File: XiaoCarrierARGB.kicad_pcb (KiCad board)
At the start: 2 copper layers, 76.4 x 50.8 mm, 24 parts, among them J1 V_{IN}^{10-24V}, J2 Conn_01x08, J3 Conn_01x01, J4 Conn_01x08, J5 Conn_01x01, J6 Conn_01x06, U1 TLV75733PDBV, U2 TPP362083-T6TR, U3 XIAO-ESP32-C6-DIP, U4 74LVC1T45W6-7, U5 74LVC1T45W6-7, U6 74LVC1T45W6-7

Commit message: adjusted prelim layout
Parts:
- moved U4 35.2 mm to (131.8, 113.3)
- moved U5 35.0 mm to (131.8, 108.5)
- moved U6 35.0 mm to (131.8, 103.6)
- moved C4 33.4 mm to (114.2, 93.5), turned to 90 degrees
- moved J6 33.2 mm to (148.8, 105.0)
- moved J4 32.4 mm to (125.2, 83.0)
- moved U3 32.0 mm to (117.4, 106.6)
- moved J3 30.1 mm to (121.2, 83.0)
- moved U1 29.3 mm to (118.1, 93.6), turned to 0 degrees
- moved F1 28.2 mm to (93.2, 100.0)
- moved J2 28.1 mm to (99.5, 83.0)
- moved J5 27.1 mm to (95.2, 83.0)
- moved D1 27.0 mm to (102.8, 108.0)
- moved R2 26.3 mm to (98.3, 101.5), turned to 180 degrees
- moved C1 25.8 mm to (121.8, 93.5), turned to -90 degrees
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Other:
- board size 76.4 x 50.8 mm -> 63.5 x 38.1 mm

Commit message: moved to 4 layers
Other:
- copper layers 2 -> 4
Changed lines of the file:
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@@
 	(layers
 		(0 "F.Cu" signal)
+		(4 "In1.Cu" power)
+		(6 "In2.Cu" power)
 		(2 "B.Cu" signal)
 		(9 "F.Adhes" user "F.Adhesive")
@@
 			)
 			(layer "dielectric 1"
+				(type "prepreg")
+				(thickness 0.1)
+				(material "FR4")
+				(epsilon_r 4.5)
+				(loss_tangent 0.02)
+			)
+			(layer "In1.Cu"
+				(type "copper")
+				(thickness 0.035)
+			)
+			(layer "dielectric 2"
 				(type "core")
-				(thickness 1.51)
+				(thickness 1.24)
+				(material "FR4")
+				(epsilon_r 4.5)
+				(loss_tangent 0.02)
+			)
+			(layer "In2.Cu"
+				(type "copper")
+				(thickness 0.035)
+			)
+			(layer "dielectric 3"
+				(type "prepreg")
+				(thickness 0.1)
 				(material "FR4")
 				(epsilon_r 4.5)
@@
 		(capping no)
 		(filling no)
+		(zone_defaults)
 		(grid_origin 88.25 119.05)
 		(pcbplotparams

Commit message: realigned schem grid added netclass assignment and net names
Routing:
- added copper zone on In1.Cu, net GND
- added copper zone on In2.Cu, net GND
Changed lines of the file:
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@@
 		(capping no)
 		(filling no)
-		(zone_defaults)
 		(grid_origin 88.25 119.05)
 		(pcbplotparams
@@
 		(layer "Edge.Cuts")
 	)
+	(zone
+		(net "GND")
+		(layers "In1.Cu" "In2.Cu")
+		(name "GND")
+		(hatch edge 0.5)
+		(connect_pads
+			(clearance 0.5)
+		)
+		(min_thickness 0.25)
+		(fill yes
+			(thermal_gap 0.5)
+			(thermal_bridge_width 0.5)
+			(island_removal_mode 0)
+		)
+		(polygon
+			(pts
+				(xy 85.25 77.55) (xy 152.75 77.55) (xy 152.75 120.55) (xy 85.75 120.55)
+			)
+		)
+	)
 	(embedded_fonts no)

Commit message: started prettying it up a bit
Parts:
- moved F1 0.45 mm to (92.8, 100.0)
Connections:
- net Net-(J1-Pin_1) renamed /V_{IN}
- net Net-(J2-Pin_3) renamed /GPIO17
- net Net-(J2-Pin_4) renamed /GPIO19
- net Net-(J2-Pin_7) renamed /GPIO20
- net Net-(J2-Pin_8) renamed /GPIO18
- net Net-(J4-Pin_3) renamed /GPIO16
- net Net-(J4-Pin_4) renamed /GPIO23
- net Net-(J4-Pin_7) renamed /GPIO22
- net Net-(J4-Pin_8) renamed /GPIO21
- net Net-(J6-Pin_1) renamed /LED_DATA^{1}
- net Net-(J6-Pin_3) renamed /LED_DATA^{2}
- net Net-(J6-Pin_5) renamed /LED_DATA^{3}
- net Net-(U2-EN) renamed /V_{IN}_{FUSED}
- net Net-(U2-SW) renamed /SWITCHNODE
- net Net-(U2-VBST) renamed /BOOTSTRAP
- net Net-(U2-VFB) renamed /FB_{BUCK}
- net Net-(U3-GPIO0_D0) renamed /GPIO0
- net Net-(U3-GPIO1_D1) renamed /GPIO1
- net Net-(U3-GPIO2_D2) renamed /GPIO2
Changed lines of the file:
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@@
 			(layers "F.Cu" "F.Mask" "F.Paste")
 			(roundrect_rratio 0.25)
-			(net "Net-(J6-Pin_3)")
+			(net "/LED_DATA^{2}")
 			(pinfunction "A_3")
 			(pintype "bidirectional")
@@
 			(layers "F.Cu" "F.Mask" "F.Paste")
 			(roundrect_rratio 0.25)
-			(net "Net-(U3-GPIO1_D1)")
+			(net "/GPIO1")
 			(pinfunction "B_4")
 			(pintype "bidirectional")
@@
 			(layers "*.Cu" "*.Mask")
 			(remove_unused_layers no)
-			(net "Net-(J1-Pin_1)")
+			(net "/V_{IN}")
 			(pinfunction "Pin_1_1")
 			(pintype "passive")
@@
 			(layers "F.Cu" "F.Mask" "F.Paste")
 			(roundrect_rratio 0.243902)
-			(net "Net-(U2-VFB)")
+			(net "/FB_{BUCK}")
 			(pintype "passive")
 		)
@@
 			(layers "F.Cu" "F.Mask" "F.Paste")
 			(roundrect_rratio 0.212766)
-			(net "Net-(U2-EN)")
+			(net "/V_{IN}_{FUSED}")
 			(pintype "passive")
 		)
@@
 			(layers "F.Cu" "F.Mask" "F.Paste")
 			(roundrect_rratio 0.125)
-			(net "Net-(U2-SW)")
+			(net "/SWITCHNODE")
 			(pinfunction "1_1")
 			(pintype "passive")
@@
 			(layers "*.Cu" "*.Mask")
 			(remove_unused_layers no)
-			(net "Net-(J4-Pin_3)")
+			(net "/GPIO16")
 			(pinfunction "Pin_3_3")
 			(pintype "passive")
@@
 			(layers "*.Cu" "*.Mask")
 			(remove_unused_layers no)
-			(net "Net-(J4-Pin_4)")
+			(net "/GPIO23")
 			(pinfunction "Pin_4_4")
 			(pintype "passive")
@@
 			(layers "*.Cu" "*.Mask")
 			(remove_unused_layers no)
-			(net "Net-(J4-Pin_7)")
+			(net "/GPIO22")
 			(pinfunction "Pin_7_7")
 			(pintype "passive")
@@
 			(layers "*.Cu" "*.Mask")
 			(remove_unused_layers no)
-			(net "Net-(J4-Pin_8)")
+			(net "/GPIO21")
 			(pinfunction "Pin_8_8")
 			(pintype "passive")
@@
 			(layers "*.Cu" "*.Mask")
 			(remove_unused_layers no)
-			(net "Net-(J2-Pin_3)")
+			(net "/GPIO17")
 			(pinfunction "Pin_3_3")
 			(pintype "passive")
@@
 			(layers "*.Cu" "*.Mask")
 			(remove_unused_layers no)
-			(net "Net-(J2-Pin_4)")
+			(net "/GPIO19")
 			(pinfunction "Pin_4_4")
 			(pintype "passive")
@@
 			(layers "*.Cu" "*.Mask")
 			(remove_unused_layers no)
-			(net "Net-(J2-Pin_7)")
+			(net "/GPIO20")
 			(pinfunction "Pin_7_7")
 			(pintype "passive")
@@
 			(layers "*.Cu" "*.Mask")
 			(remove_unused_layers no)
-			(net "Net-(J2-Pin_8)")
+			(net "/GPIO18")
 			(pinfunction "Pin_8_8")
 			(pintype "passive")
@@
 	(footprint "Fuse:Fuse_1812_4532Metric"
 		(layer "F.Cu")
-		(at 93.25 100.05 90)
+		(at 92.803052 100.05 90)
 		(descr "Fuse SMD 1812 (4532 Metric), square (rectangular) end terminal, IPC-7351 nominal, (Body size source: https://www.nikhef.nl/pub/departments/mt/projects/detectorR_D/dtddice/ERJ2G.pdf)")
 		(tags "fuse")
@@
 			(layers "F.Cu" "F.Mask" "F.Paste")
 			(roundrect_rratio 0.222222)
-			(net "Net-(J1-Pin_1)")
+			(net "/V_{IN}")
 			(pintype "passive")
 		)
@@
 			(layers "F.Cu" "F.Mask" "F.Paste")
 			(roundrect_rratio 0.222222)
-			(net "Net-(U2-EN)")
+			(net "/V_{IN}_{FUSED}")
 			(pintype "passive")
 		)
@@
 			(layers "F.Cu" "F.Mask" "F.Paste")
 			(roundrect_rratio 0.25)
-			(net "Net-(J6-Pin_5)")
+			(net "/LED_DATA^{3}")
 			(pinfunction "A_3")
 			(pintype "bidirectional")
@@
 			(layers "F.Cu" "F.Mask" "F.Paste")
 			(roundrect_rratio 0.25)
-			(net "Net-(U3-GPIO2_D2)")
+			(net "/GPIO2")
 			(pinfunction "B_4")
 			(pintype "bidirectional")
@@
 			(layers "F.Cu" "F.Mask" "F.Paste")
 			(roundrect_rratio 0.243902)
-			(net "Net-(U2-VFB)")
+			(net "/FB_{BUCK}")
 			(pintype "passive")
 		)
@@
 			(layers "F.Cu" "F.Mask")
 			(roundrect_rratio 0.1)
-			(net "Net-(U3-GPIO0_D0)")
+			(net "/GPIO0")
 			(pinfunction "GPIO0_D0_1")
 			(pintype "bidirectional")
@@
 			(layers "*.Cu" "*.Mask")
 			(remove_unused_layers no)
-			(net "Net-(U3-GPIO0_D0)")
+			(net "/GPIO0")
 			(pinfunction "GPIO0_D0_1")
 			(pintype "bidirectional")
@@
 			(layers "F.Cu" "F.Mask")
 			(roundrect_rratio 0.1)
-			(net "Net-(U3-GPIO1_D1)")
+			(net "/GPIO1")
 			(pinfunction "GPIO1_D1_2")
 			(pintype "bidirectional")
@@
 			(layers "*.Cu" "*.Mask")
 			(remove_unused_layers no)
-			(net "Net-(U3-GPIO1_D1)")
+			(net "/GPIO1")
 			(pinfunction "GPIO1_D1_2")
 			(pintype "bidirectional")
@@
 			(layers "F.Cu" "F.Mask")
 			(roundrect_rratio 0.1)
-			(net "Net-(U3-GPIO2_D2)")
+			(net "/GPIO2")
 			(pinfunction "GPIO2_D2_3")
 			(pintype "bidirectional")
@@
 			(layers "*.Cu" "*.Mask")
 			(remove_unused_layers no)
-			(net "Net-(U3-GPIO2_D2)")
+			(net "/GPIO2")
 			(pinfunction "GPIO2_D2_3")
 			(pintype "bidirectional")
@@
 			(layers "F.Cu" "F.Mask")
 			(roundrect_rratio 0.1)
-			(net "Net-(J4-Pin_8)")
+			(net "/GPIO21")
 			(pinfunction "GPIO21_D3_4")
 			(pintype "passive")
@@
 			(layers "*.Cu" "*.Mask")
 			(remove_unused_layers no)
-			(net "Net-(J4-Pin_8)")
+			(net "/GPIO21")
 			(pinfunction "GPIO21_D3_4")
 			(pintype "passive")
@@
 			(layers "F.Cu" "F.Mask")
 			(roundrect_rratio 0.1)
-			(net "Net-(J4-Pin_7)")
+			(net "/GPIO22")
 			(pinfunction "GPIO22_D4_5")
 			(pintype "bidirectional")
@@
 			(layers "*.Cu" "*.Mask")
 			(remove_unused_layers no)
-			(net "Net-(J4-Pin_7)")
+			(net "/GPIO22")
 			(pinfunction "GPIO22_D4_5")
 			(pintype "bidirectional")
@@
 			(layers "F.Cu" "F.Mask")
 			(roundrect_rratio 0.1)
-			(net "Net-(J4-Pin_4)")
+			(net "/GPIO23")
 			(pinfunction "GPIO23_D5_6")
 			(pintype "bidirectional")
@@
 			(layers "*.Cu" "*.Mask")
 			(remove_unused_layers no)
-			(net "Net-(J4-Pin_4)")
+			(net "/GPIO23")
 			(pinfunction "GPIO23_D5_6")
 			(pintype "bidirectional")
@@
 			(layers "F.Cu" "F.Mask")
 			(roundrect_rratio 0.1)
-			(net "Net-(J4-Pin_3)")
+			(net "/GPIO16")
 			(pinfunction "GPIO16_D6_7")
 			(pintype "bidirectional")
@@
 			(layers "*.Cu" "*.Mask")
 			(remove_unused_layers no)
-			(net "Net-(J4-Pin_3)")
+			(net "/GPIO16")
 			(pinfunction "GPIO16_D6_7")
 			(pintype "bidirectional")
@@
 			(layers "*.Cu" "*.Mask")
 			(remove_unused_layers no)
-			(net "Net-(J2-Pin_3)")
+			(net "/GPIO17")
 			(pinfunction "GPIO17_D7_8")
 			(pintype "bidirectional")
@@
 			(layers "F.Cu" "F.Mask")
 			(roundrect_rratio 0.1)
-			(net "Net-(J2-Pin_3)")
+			(net "/GPIO17")
 			(pinfunction "GPIO17_D7_8")
 			(pintype "bidirectional")
@@
 			(layers "*.Cu" "*.Mask")
 			(remove_unused_layers no)
-			(net "Net-(J2-Pin_4)")
+			(net "/GPIO19")
 			(pinfunction "GPIO19_D8_9")
 			(pintype "bidirectional")
@@
 			(layers "F.Cu" "F.Mask")
 			(roundrect_rratio 0.1)
-			(net "Net-(J2-Pin_4)")
+			(net "/GPIO19")
 			(pinfunction "GPIO19_D8_9")
 			(pintype "bidirectional")
@@
 			(layers "*.Cu" "*.Mask")
 			(remove_unused_layers no)
-			(net "Net-(J2-Pin_7)")
+			(net "/GPIO20")
 			(pinfunction "GPIO20_D9_10")
 			(pintype "bidirectional")
@@
 			(layers "F.Cu" "F.Mask")
 			(roundrect_rratio 0.1)
-			(net "Net-(J2-Pin_7)")
+			(net "/GPIO20")
 			(pinfunction "GPIO20_D9_10")
 			(pintype "bidirectional")
@@
 			(layers "*.Cu" "*.Mask")
 			(remove_unused_layers no)
-			(net "Net-(J2-Pin_8)")
+			(net "/GPIO18")
 			(pinfunction "GPIO18_D10_11")
 			(pintype "bidirectional")
@@
 			(layers "F.Cu" "F.Mask")
 			(roundrect_rratio 0.1)
-			(net "Net-(J2-Pin_8)")
+			(net "/GPIO18")
 			(pinfunction "GPIO18_D10_11")
 			(pintype "bidirectional")
@@
 			(layers "F.Cu" "F.Mask" "F.Paste")
 			(roundrect_rratio 0.25)
-			(net "Net-(J6-Pin_1)")
+			(net "/LED_DATA^{1}")
 			(pinfunction "A_3")
 			(pintype "bidirectional")
@@
 			(layers "F.Cu" "F.Mask" "F.Paste")
 			(roundrect_rratio 0.25)
-			(net "Net-(U3-GPIO0_D0)")
+			(net "/GPIO0")
 			(pinfunction "B_4")
 			(pintype "bidirectional")
@@
 			(layers "*.Cu" "*.Mask")
 			(remove_unused_layers no)
-			(net "Net-(J6-Pin_1)")
+			(net "/LED_DATA^{1}")
 			(pinfunction "Pin_1_1")
 			(pintype "passive")
@@
 			(layers "*.Cu" "*.Mask")
 			(remove_unused_layers no)
-			(net "Net-(J6-Pin_3)")
+			(net "/LED_DATA^{2}")
 			(pinfunction "Pin_3_3")
 			(pintype "passive")
@@
 			(layers "*.Cu" "*.Mask")
 			(remove_unused_layers no)
-			(net "Net-(J6-Pin_5)")
+			(net "/LED_DATA^{3}")
 			(pinfunction "Pin_5_5")
 			(pintype "passive")
@@
 			(layers "F.Cu" "F.Mask" "F.Paste")
 			(roundrect_rratio 0.25)
-			(net "Net-(U2-SW)")
+			(net "/SWITCHNODE")
 			(pinfunction "SW_2")
 			(pintype "power_out")
@@
 			(layers "F.Cu" "F.Mask" "F.Paste")
 			(roundrect_rratio 0.25)
-			(net "Net-(U2-EN)")
+			(net "/V_{IN}_{FUSED}")
 			(pinfunction "VIN_3")
 			(pintype "power_in")
@@
 			(layers "F.Cu" "F.Mask" "F.Paste")
 			(roundrect_rratio 0.25)
-			(net "Net-(U2-VFB)")
+			(net "/FB_{BUCK}")
 			(pinfunction "VFB_4")
 			(pintype "input")
@@
 			(layers "F.Cu" "F.Mask" "F.Paste")
 			(roundrect_rratio 0.25)
-			(net "Net-(U2-EN)")
+			(net "/V_{IN}_{FUSED}")
 			(pinfunction "EN_5")
 			(pintype "input")
@@
 			(layers "F.Cu" "F.Mask" "F.Paste")
 			(roundrect_rratio 0.25)
-			(net "Net-(U2-VBST)")
+			(net "/BOOTSTRAP")
 			(pinfunction "VBST_6")
 			(pintype "power_out")
@@
 			(layers "F.Cu" "F.Mask" "F.Paste")
 			(roundrect_rratio 0.212766)
-			(net "Net-(U2-VBST)")
+			(net "/BOOTSTRAP")
 			(pintype "passive")
 		)
@@
 			(layers "F.Cu" "F.Mask" "F.Paste")
 			(roundrect_rratio 0.212766)
-			(net "Net-(U2-SW)")
+			(net "/SWITCHNODE")
 			(pintype "passive")
 		)
@@
 			(layers "F.Cu" "F.Mask" "F.Paste")
 			(roundrect_rratio 0.212766)
-			(net "Net-(U2-EN)")
+			(net "/V_{IN}_{FUSED}")
 			(pintype "passive")
 		)

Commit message: Did mostly all layout need to sanity check and review
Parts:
- added REF**: SerbTek mark, Custom_Library:SerbTek mark, F.Cu at (139.8, 118.0)
- added RT**: RT-NY, RT-NY:RT-NY-Patch, B.Cu at (140.5, 102.0)
- moved C1 5.28 mm to (118.0, 89.8), turned to 0 degrees
- moved C6 1.00 mm to (109.8, 91.1)
- moved C7 1.00 mm to (109.8, 94.2)
- moved U6 0.55 mm to (131.8, 103.0), turned to 180 degrees
- moved U5 0.47 mm to (131.8, 108.1), turned to 180 degrees
- moved U1 0.29 mm to (118.0, 93.3), turned to 90 degrees
- moved U4 0.25 mm to (131.8, 113.0), turned to 180 degrees
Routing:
- net +5V: track 0.00 -> 125.3 mm, vias 0 -> 10
- net +3V3: track 0.00 -> 50.2 mm
- net /Xiao3v3: track 0.00 -> 39.0 mm, vias 0 -> 3
- net /LDO_{in}: track 0.00 -> 38.6 mm
- net /GPIO21: track 0.00 -> 32.0 mm
- net /GPIO18: track 0.00 -> 28.4 mm
- net /GPIO22: track 0.00 -> 27.4 mm
- net /GPIO20: track 0.00 -> 24.4 mm
- net /GPIO19: track 0.00 -> 23.1 mm
- net /GPIO23: track 0.00 -> 21.7 mm
- net /GPIO17: track 0.00 -> 19.2 mm
- net /LED_DATA^{3}: track 0.00 -> 18.9 mm
- net /LED_DATA^{2}: track 0.00 -> 18.9 mm
- net /LED_DATA^{1}: track 0.00 -> 18.8 mm
- net /GPIO16: track 0.00 -> 18.2 mm
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- added copper zone on F.Cu, net +5V
- added copper zone on In2.Cu, net +5V
- added copper zone on F.Cu, net /BOOTSTRAP
- added copper zone on F.Cu, net /SWITCHNODE
- added copper zone on B.Cu, net GND
- added copper zone on F.Cu, net GND

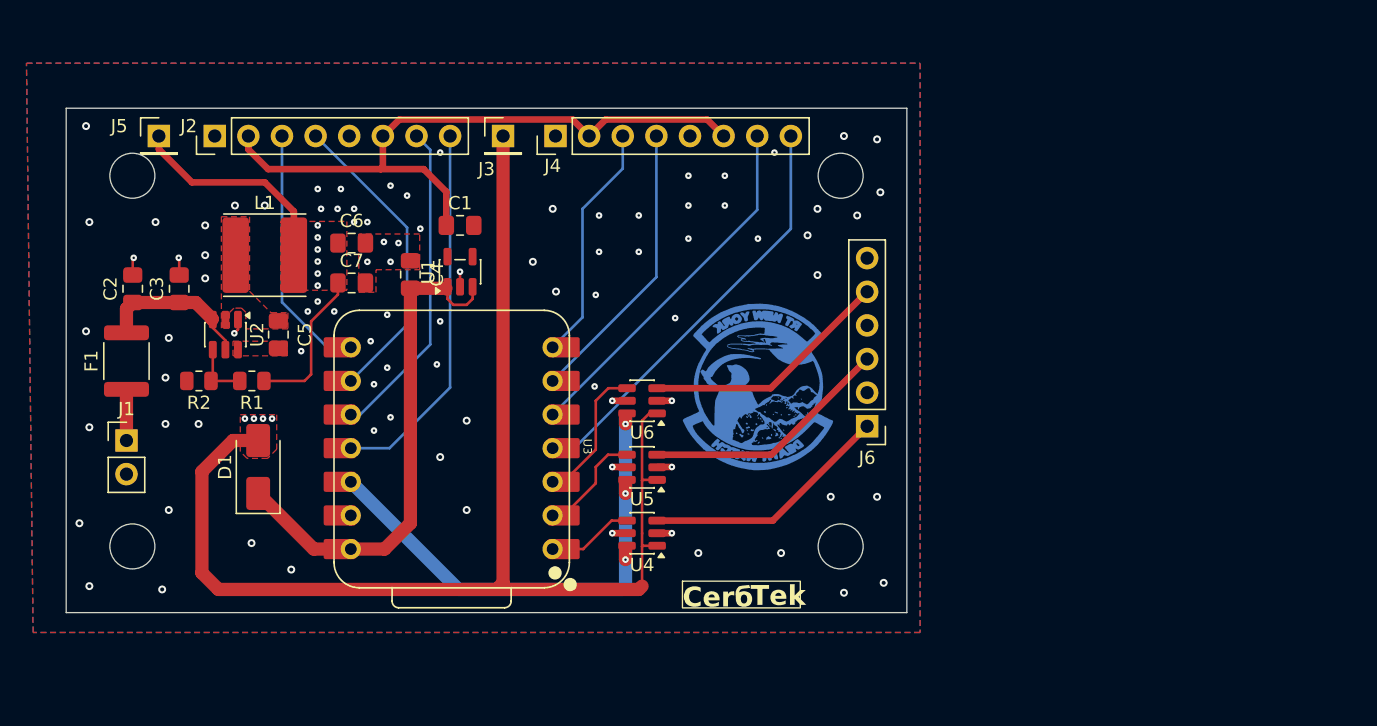
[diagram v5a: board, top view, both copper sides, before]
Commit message: Refactored layout, added jumpers and unpopulated pull up/down Rs to backside of board
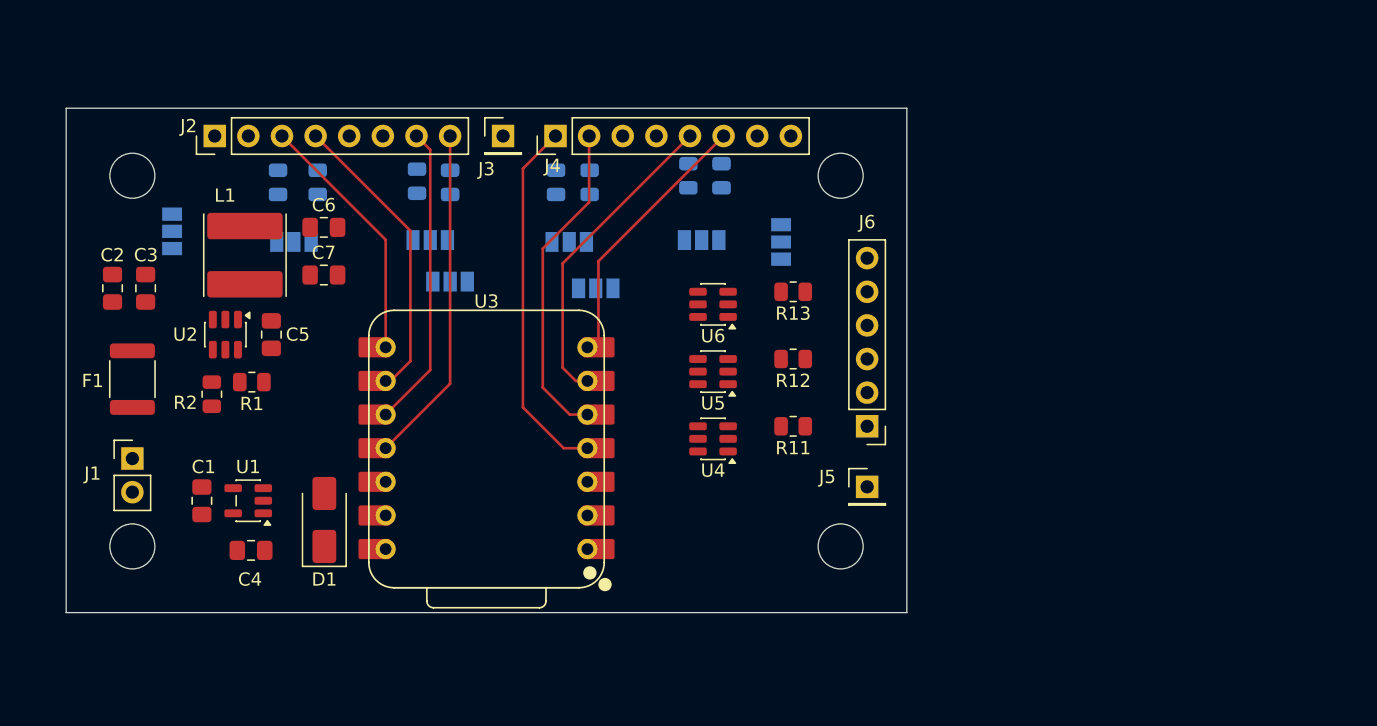
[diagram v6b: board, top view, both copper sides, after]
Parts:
- removed REF**: SerbTek mark, Custom_Library:SerbTek mark
- removed RT**: RT-NY, RT-NY:RT-NY-Patch
- added JP10: SolderJumper_3_Open, Jumper:SolderJumper-3_P1.3mm_Open_Pad1.0x1.5mm, B.Cu at (96.2, 90.2)
- added JP11: SolderJumper_3_Open, Jumper:SolderJumper-3_P1.3mm_Open_Pad1.0x1.5mm, B.Cu at (105.5, 91.0)
- added JP12: SolderJumper_3_Open, Jumper:SolderJumper-3_P1.3mm_Open_Pad1.0x1.5mm, B.Cu at (128.2, 94.5)
- added JP13: SolderJumper_3_Open, Jumper:SolderJumper-3_P1.3mm_Open_Pad1.0x1.5mm, B.Cu at (126.2, 91.0)
- added JP14: SolderJumper_3_Open, Jumper:SolderJumper-3_P1.3mm_Open_Pad1.0x1.5mm, B.Cu at (142.2, 91.0)
- added JP15: SolderJumper_3_Open, Jumper:SolderJumper-3_P1.3mm_Open_Pad1.0x1.5mm, B.Cu at (136.2, 90.9)
- added JP8: SolderJumper_3_Open, Jumper:SolderJumper-3_P1.3mm_Open_Pad1.0x1.5mm, B.Cu at (115.8, 90.9)
- added JP9: SolderJumper_3_Open, Jumper:SolderJumper-3_P1.3mm_Open_Pad1.0x1.5mm, B.Cu at (117.2, 94.0)
- added R10: R_Small_US, Resistor_SMD:R_0805_2012Metric, B.Cu at (137.8, 86.0)
- added R11: R_Small_US, Resistor_SMD:R_0805_2012Metric, F.Cu at (143.2, 105.0)
- added R12: R_Small_US, Resistor_SMD:R_0805_2012Metric, F.Cu at (143.2, 99.9)
- added R13: R_Small_US, Resistor_SMD:R_0805_2012Metric, F.Cu at (143.2, 94.8)
- added R3: R_Small_US, Resistor_SMD:R_0805_2012Metric, B.Cu at (117.2, 86.5)
- added R4: R_Small_US, Resistor_SMD:R_0805_2012Metric, B.Cu at (114.8, 86.5)
- added R5: R_Small_US, Resistor_SMD:R_0805_2012Metric, B.Cu at (107.2, 86.5)
- added R6: R_Small_US, Resistor_SMD:R_0805_2012Metric, B.Cu at (104.2, 86.5)
- added R7: R_Small_US, Resistor_SMD:R_0805_2012Metric, B.Cu at (127.8, 86.5)
- added R8: R_Small_US, Resistor_SMD:R_0805_2012Metric, B.Cu at (125.2, 86.5)
- added R9: R_Small_US, Resistor_SMD:R_0805_2012Metric, B.Cu at (135.2, 86.0)
- moved J5 59.7 mm to (148.8, 109.5)
- moved C1 28.5 mm to (98.5, 110.6), turned to 90 degrees
- moved C4 24.1 mm to (102.2, 114.3), turned to 180 degrees
- moved U1 23.6 mm to (102.0, 110.6), turned to 180 degrees
- moved U6 9.05 mm to (137.1, 95.8)
- moved U5 9.00 mm to (137.1, 100.8)
- moved U4 8.92 mm to (137.1, 105.9)
- moved D1 6.40 mm to (107.8, 112.0)
- moved U3 2.63 mm to (120.0, 106.6)
- moved C3 2.54 mm to (94.2, 94.5)
- moved C6 2.41 mm to (107.7, 90.0)
- moved C7 2.18 mm to (107.7, 93.5)
- moved C2 1.53 mm to (91.8, 94.5)
- moved L1 1.50 mm to (101.8, 92.0), turned to 90 degrees
- moved F1 1.43 mm to (93.2, 101.4)
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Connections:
- J4 pad 1: GND -> /GPIO21
- J4 pad 2: +3V3 -> /GPIO22
- J4 pad 3: /GPIO16 -> +3V3
- J4 pad 4: /GPIO23 -> GND
- J4 pad 5: GND -> /GPIO23
- J4 pad 6: +3V3 -> /GPIO16
- J4 pad 7: /GPIO22 -> +3V3
- J4 pad 8: /GPIO21 -> GND
- J6 pad 1: /LED_DATA^{1} -> Net-(J6-Pin_1)
- J6 pad 3: /LED_DATA^{2} -> Net-(J6-Pin_3)
- J6 pad 5: /LED_DATA^{3} -> Net-(J6-Pin_5)
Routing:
- net +5V: track 125.3 -> 0.00 mm, vias 10 -> 0
- net +3V3: track 50.2 -> 0.00 mm
- net /Xiao3v3: track 39.0 -> 0.00 mm, vias 3 -> 0
- net /LDO_{in}: track 38.6 -> 0.00 mm
- net /LED_DATA^{3}: track 18.9 -> 0.00 mm
- net /LED_DATA^{2}: track 18.9 -> 0.00 mm
- net /LED_DATA^{1}: track 18.8 -> 0.00 mm
- net /V_{IN}_{FUSED}: track 11.7 -> 0.00 mm
- net GND: track 11.6 -> 0.00 mm, vias 90 -> 0
- net /GPIO2: track 9.88 -> 0.00 mm
- net /GPIO1: track 7.41 -> 0.00 mm
- net /GPIO0: track 5.68 -> 0.00 mm
- net /FB_{BUCK}: track 4.59 -> 0.00 mm
- net /GPIO21: track 32.0 -> 27.7 mm
- net /V_{IN}: track 3.86 -> 0.00 mm
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- removed copper zone on F.Cu, net +5V
- removed copper zone on In2.Cu, net +5V
- removed copper zone on F.Cu, net /BOOTSTRAP
- removed copper zone on F.Cu, net /SWITCHNODE
- removed copper zone on B.Cu, net GND
- removed copper zone on F.Cu, net GND
